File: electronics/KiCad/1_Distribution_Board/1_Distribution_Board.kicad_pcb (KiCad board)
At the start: 2 copper layers, 130 x 120 mm, 149 parts, among them CN1 HC-5264-3A, CN2 HC-5264-3A, J1 JST VH, J10 Generic 2.54mm, J11 Generic 2.54mm, J12 Conn_01x06, J13 Conn_01x10, J17 Conn_02x08_Odd_Even, J2 JST VH, J23 JST PH, J24 Generic 2.54mm, J27 JST PH, J28 Generic 2.54mm, J3 JST VH, J31 JST PH, J32 Generic 2.54mm, J35 JST PH, J36 Generic 2.54mm, J39 JST PH, J4 Conn_01x04, J40 Generic 2.54mm, J5 Generic 2.54mm, J6 Generic 2.54mm, J8 Generic 2.54mm, J9 Generic 2.54mm, M1 MountingHole_3.2mm_M3_ISO7380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, P1 Header-Female-2.54_1x8, P10 Header-Female-2.54_1x8, P11 Header-Female-2.54_1x2, P12 Header-Female-2.54_1x8, P13 Header-Female-2.54_1x8, P14 Header-Female-2.54_1x2, P15 Header-Female-2.54_1x8, P2 Header-Female-2.54_1x2, P3 Header-Female-2.54_1x8, P4 Header-Female-2.54_1x8, P5 Header-Female-2.54_1x2, P6 Header-Female-2.54_1x8, P7 Header-Female-2.54_1x8, P8 Header-Female-2.54_1x2, P9 Header-Female-2.54_1x8, Q1 DMG2305UX, Q2 AO3400A, Q3 AO3400A, Q4 AO3400A, Q5 AO3400A, U1 KH-2.54FH-1X20P-H8.5, U2 KH-2.54FH-1X20P-H8.5, U3 R-78C5.0-1.0, U4 R-78B12-2.0, U5 R-78B6.5-1.5, U6 PCA9306, U7 PCA9685PW, Y1 25MHz

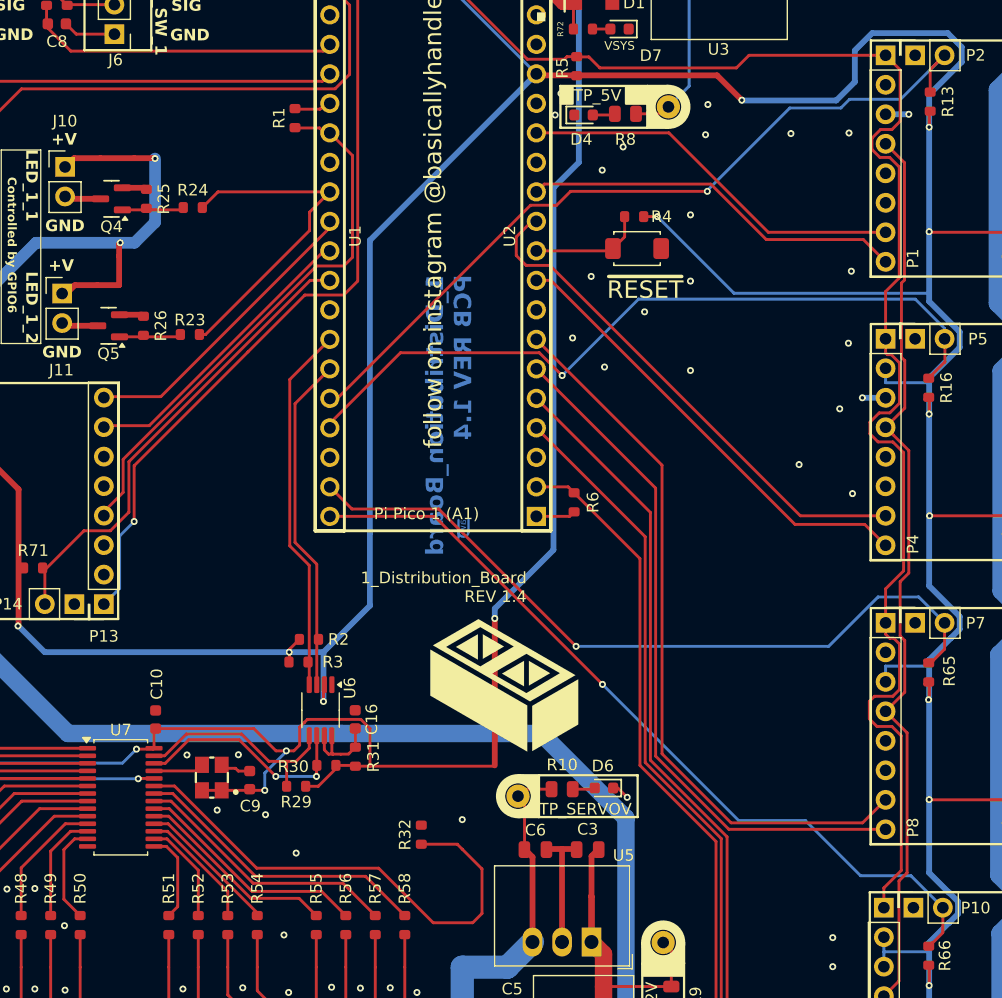
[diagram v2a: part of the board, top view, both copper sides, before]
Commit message: distribution board v1.4: s1 on the silkscreen, ground stitching, small cleanups
Small fixes from a review of the v1.4 layout:

- The RESET button's reference, S1, is now printed on the top silkscreen,
  upright and left of the button, as proposed in #953. It is at least
  1.5 mm from every pad and clear of the RESET label. An assembly order
  was flagged earlier for the missing S1 marking.
- Y1 loses the PROD_ID field "XTAL-25500" left over from the SparkFun
  symbol, in the schematic and on the board. Its MPN, manufacturer, LCSC
  number and datasheet stay.
- The bottom-layer +3V3 strap to driver A4's MS2 pin (P7.3) now runs at
  y = 88.9 mm instead of 88.7 mm. It cleared the GND pin P7.2 by 0.21 mm;
  it now clears it by 0.41 mm.
- Removed a 0.12 mm VSYS track stub that lay entirely inside Y1 pad 1.
- Removed an unused copy of the old outline-only logo from User.Drawings,
  outside the board outline, so plotting that layer no longer prints it.
- The VSYS link that ran down the top layer under the logo is re-routed
  around its left side: the bottom-layer run continues at 45 degrees to
  y = 84 mm and left to a via at (83.5, 84.0), then a 0.5 mm top-layer
  track runs down x = 83.5 mm to the existing VSYS track at y = 97.32 mm.
  The ground pour under the logo is now one unbroken piece, with no
  clearance channels showing through the white silkscreen. The new path
  is about as long as the old one.
- Seven 0.6/0.3 mm GND vias stitch ground pour patches that joined the
  rest of ground at a single point, left where the jumper fields and the
  module headers were removed: two beside P1 pin 2 on the bottom layer,
  one beside P7 pin 2 on the bottom layer, one beside P13 pins 2 and 3 on
  the top layer, and one at the top end of each of the three top-layer
  ground strips between the PWM tracks below R55-R58.

DRC (zones refilled, all severities, schematic parity) shows the same
items as before and no unconnected items. ERC is unchanged. The netlist
is unchanged apart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
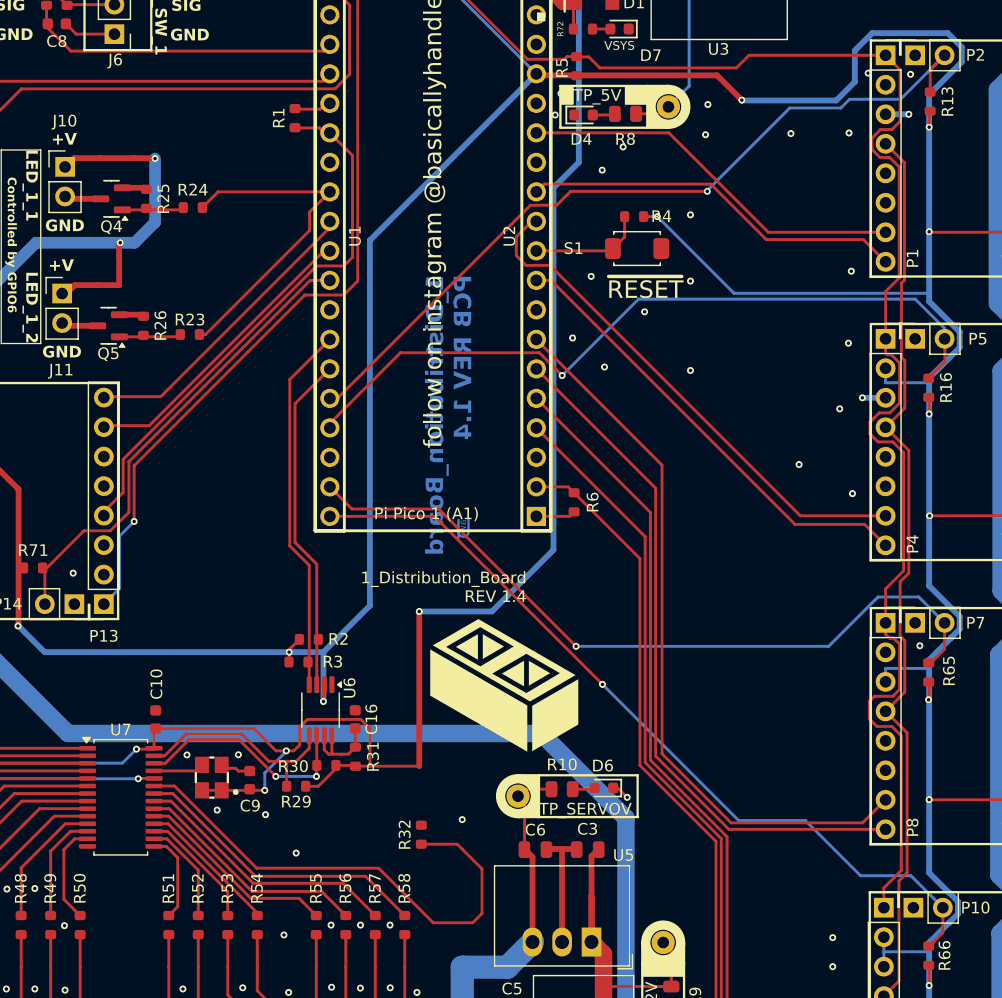
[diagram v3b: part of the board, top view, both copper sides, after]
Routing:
- net GND: vias 59 -> 66
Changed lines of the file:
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@@
 		(at 102.25 52.75 180)
 		(property "Reference" "S1"
-			(at 0.425 -2.635 0)
+			(at 5.45 0 0)
 			(layer "F.SilkS")
-			(hide yes)
 			(effects
 				(font
@@
 			)
 		)
-		(property "PROD_ID" "XTAL-25500"
-			(at 0 0 90)
-			(unlocked yes)
-			(layer "F.Fab")
-			(hide yes)
-			(effects
-				(font
-					(size 1 1)
-					(thickness 0.15)
-				)
-			)
-		)
 		(property "LCSC" "C41361435"
 			(at 0 0 90)
@@
 		(layer "F.SilkS")
 	)
-	(gr_poly
-		(pts
-			(xy 185.9818 169.912928) (xy 183.678231 171.283258) (xy 181.322042 169.943513) (xy 181.990296 169.943513)
-			(xy 183.513661 170.823094) (xy 183.513661 169.063933) (xy 183.845765 169.063933) (xy 183.845765 170.772294)
-			(xy 185.315262 169.914938) (xy 183.845765 169.063932) (xy 183.845765 169.063933) (xy 183.513661 169.063933)
-			(xy 183.513661 169.063932) (xy 181.990296 169.943513) (xy 181.322042 169.943513) (xy 181.321112 169.942984)
-			(xy 183.677914 168.582285)
-		)
-		(stroke
-			(width 0)
-			(type solid)
-		)
-		(fill yes)
-		(layer "Dwgs.User")
-	)
-	(gr_poly
-		(pts
-			(xy 186.854501 170.419128) (xy 189.158387 171.749665) (xy 186.854925 173.1201) (xy 184.498443 171.78025)
-			(xy 185.166883 171.78025) (xy 186.690354 172.659831) (xy 186.690354 172.609137) (xy 187.022459 172.609137)
-			(xy 188.491849 171.751675) (xy 187.022459 170.900776) (xy 187.022459 172.609137) (xy 186.690354 172.609137)
-			(xy 186.690354 170.900775) (xy 185.166883 171.78025) (xy 184.498443 171.78025) (xy 184.497699 171.779827)
-			(xy 186.854501 170.419128)
-		)
-		(stroke
-			(width 0)
-			(type solid)
-		)
-		(fill yes)
-		(layer "Dwgs.User")
-	)
-	(gr_poly
-		(pts
-			(xy 190.760492 171.807556) (xy 190.760492 175.485793) (xy 187.052198 177.625426) (xy 179.895325 173.497608)
-			(xy 179.895325 173.299911) (xy 180.230393 173.299911) (xy 186.915038 177.159335) (xy 186.915038 174)
-			(xy 187.25 174) (xy 187.25 177.125681) (xy 190.424153 175.29307) (xy 190.424153 172.16739) (xy 187.25 174)
-			(xy 186.915038 174) (xy 186.915038 173.97661) (xy 180.230393 170.117292) (xy 180.230393 173.299911)
-			(xy 179.895325 173.299911) (xy 179.895325 169.835775) (xy 180.41285 169.835775) (xy 187.102787 173.698162)
-			(xy 190.237781 171.888201) (xy 183.546786 168.025178) (xy 180.41285 169.835775) (xy 179.895325 169.835775)
-			(xy 179.895325 169.75005) (xy 183.528795 167.62788)
-		)
-		(stroke
-			(width 0)
-			(type solid)
-		)
-		(fill yes)
-		(layer "Dwgs.User")
-	)
 	(gr_line
 		(start 158.214286 75.624)
@@
 	)
 	(via
+		(at 126.6 86.95)
+		(size 0.6)
+		(drill 0.3)
+		(layers "F.Cu" "B.Cu")
+		(free yes)
+		(capping no)
+		(covering
+			(front no)
+			(back no)
+		)
+		(plugging
+			(front no)
+			(back no)
+		)
+		(filling no)
+		(net "GND")
+	)
+	(via
 		(at 75.95 116.35)
 		(size 0.6)
@@
 	)
 	(via
+		(at 80.982 111)
+		(size 0.6)
+		(drill 0.3)
+		(layers "F.Cu" "B.Cu")
+		(free yes)
+		(capping no)
+		(covering
+			(front no)
+			(back no)
+		)
+		(plugging
+			(front no)
+			(back no)
+		)
+		(filling no)
+		(net "GND")
+	)
+	(via
 		(at 73.35 121.9)
 		(size 0.6)
@@
 	)
 	(via
+		(at 75.902 111)
+		(size 0.6)
+		(drill 0.3)
+		(layers "F.Cu" "B.Cu")
+		(free yes)
+		(capping no)
+		(covering
+			(front no)
+			(back no)
+		)
+		(plugging
+			(front no)
+			(back no)
+		)
+		(filling no)
+		(net "GND")
+	)
+	(via
+		(at 125.8 37.75)
+		(size 0.6)
+		(drill 0.3)
+		(layers "F.Cu" "B.Cu")
+		(free yes)
+		(capping no)
+		(covering
+			(front no)
+			(back no)
+		)
+		(plugging
+			(front no)
+			(back no)
+		)
+		(filling no)
+		(net "GND")
+	)
+	(via
 		(at 72.25 116.8)
 		(size 0.6)
@@
 	)
 	(via
+		(at 53.7 80.7)
+		(size 0.6)
+		(drill 0.3)
+		(layers "F.Cu" "B.Cu")
+		(free yes)
+		(capping no)
+		(covering
+			(front no)
+			(back no)
+		)
+		(plugging
+			(front no)
+			(back no)
+		)
+		(filling no)
+		(net "GND")
+	)
+	(via
+		(at 122.15 37.65)
+		(size 0.6)
+		(drill 0.3)
+		(layers "F.Cu" "B.Cu")
+		(free yes)
+		(capping no)
+		(covering
+			(front no)
+			(back no)
+		)
+		(plugging
+			(front no)
+			(back no)
+		)
+		(filling no)
+		(net "GND")
+	)
+	(via
 		(at 50.4 107.85)
 		(size 0.6)
@@
 	)
 	(via
+		(at 78.442 111)
+		(size 0.6)
+		(drill 0.3)
+		(layers "F.Cu" "B.Cu")
+		(free yes)
+		(capping no)
+		(covering
+			(front no)
+			(back no)
+		)
+		(plugging
+			(front no)
+			(back no)
+		)
+		(filling no)
+		(net "GND")
+	)
+	(via
 		(at 68.3 116.4)
 		(size 0.6)
@@
 	)
 	(segment
-		(start 123.65 88.7)
+		(start 123.65 88.9)
 		(end 123.65 90.055)
 		(width 0.25)
@@
 	(segment
 		(start 127.4 106.5)
-		(end 127.4 88.7)
+		(end 127.4 88.9)
 		(width 0.5)
 		(layer "B.Cu")
@@
 	)
 	(segment
-		(start 127.4 88.7)
+		(start 127.4 88.9)
 		(end 127.4 88.162075)
 		(width 0.5)
@@
 	)
 	(segment
-		(start 127.4 88.7)
-		(end 123.65 88.7)
+		(start 127.4 88.9)
+		(end 123.65 88.9)
 		(width 0.25)
 		(layer "B.Cu")
@@
 	)
 	(segment
-		(start 66.5772 99.3128)
-		(end 66.49 99.4)
-		(width 0.25)
-		(layer "F.Cu")
-		(net "VSYS")
-	)
-	(segment
 		(start 79.2544 94.075134)
 		(end 79.2544 97.32)
@@
 	)
 	(segment
-		(start 90 97.25)
-		(end 90 84.6)
+		(start 83.5 84)
+		(end 83.5 97.32)
 		(width 0.5)
 		(layer "F.Cu")
@@
 	)
 	(segment
-		(start 89.93 97.32)
-		(end 90 97.25)
-		(width 0.25)
-		(layer "F.Cu")
-		(net "VSYS")
-	)
-	(segment
 		(start 69.244702 94.08)
 		(end 71.164702 96)
@@
 	(segment
 		(start 79.2544 97.32)
-		(end 89.93 97.32)
+		(end 83.5 97.32)
 		(width 0.25)
 		(layer "F.Cu")
@@
 	)
 	(via
-		(at 90 84.6)
+		(at 83.5 84)
 		(size 0.6)
 		(drill 0.3)
@@
 	)
 	(segment
-		(start 90 84.6)
-		(end 90 83.75)
+		(start 89.75 84)
+		(end 83.5 84)
 		(width 0.5)
 		(layer "B.Cu")
@@
 	)
 	(segment
-		(start 90 83.75)
+		(start 89.75 84)
 		(end 95.05 78.7)
 		(width 0.5)
@@
 		(members "c18c1f43-2b16-4fc1-9a59-b86ec7c54358" "fac0cd4b-dc62-4271-a4c5-45b36ca86053")
 	)
-	(group ""
-		(members "86a04bf0-7eb3-4ad9-8735-edba8bfc5a84" "c703c196-366c-4ca6-9e0d-081d10e6d727"
-			"da847c9b-e65e-4264-a892-c01d93e2e40e"
-		)
-	)
 	(group "group-boardCharacteristics"
